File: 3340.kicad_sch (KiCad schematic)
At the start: 176 parts, among them J1 Conn_01x17, J10 FM1, J11 Conn_01x17, J12 V/OCT2, J13 PULSE2, J14 SAW2, J15 TRI2, J16 SINE2, J17 SYNC2, J18 Conn_01x17, J19 PWM2, J2 Conn_01x17, J20 FM2, J3 V/OCT1, J4 PULSE1, J5 SAW1, J6 TRI1, J7 SINE1, J8 SYNC1, J9 PWM1, Q1 2N3904, Q2 2N3906, Q3 2N3904, Q4 2N3906, Q5 2N3904, Q6 2N3904, SW2 DPDT_OOO, U1 TL072, U2 TL074, U3 CEM3340, U4 TL072, U5 CEM3340, U6 TL074

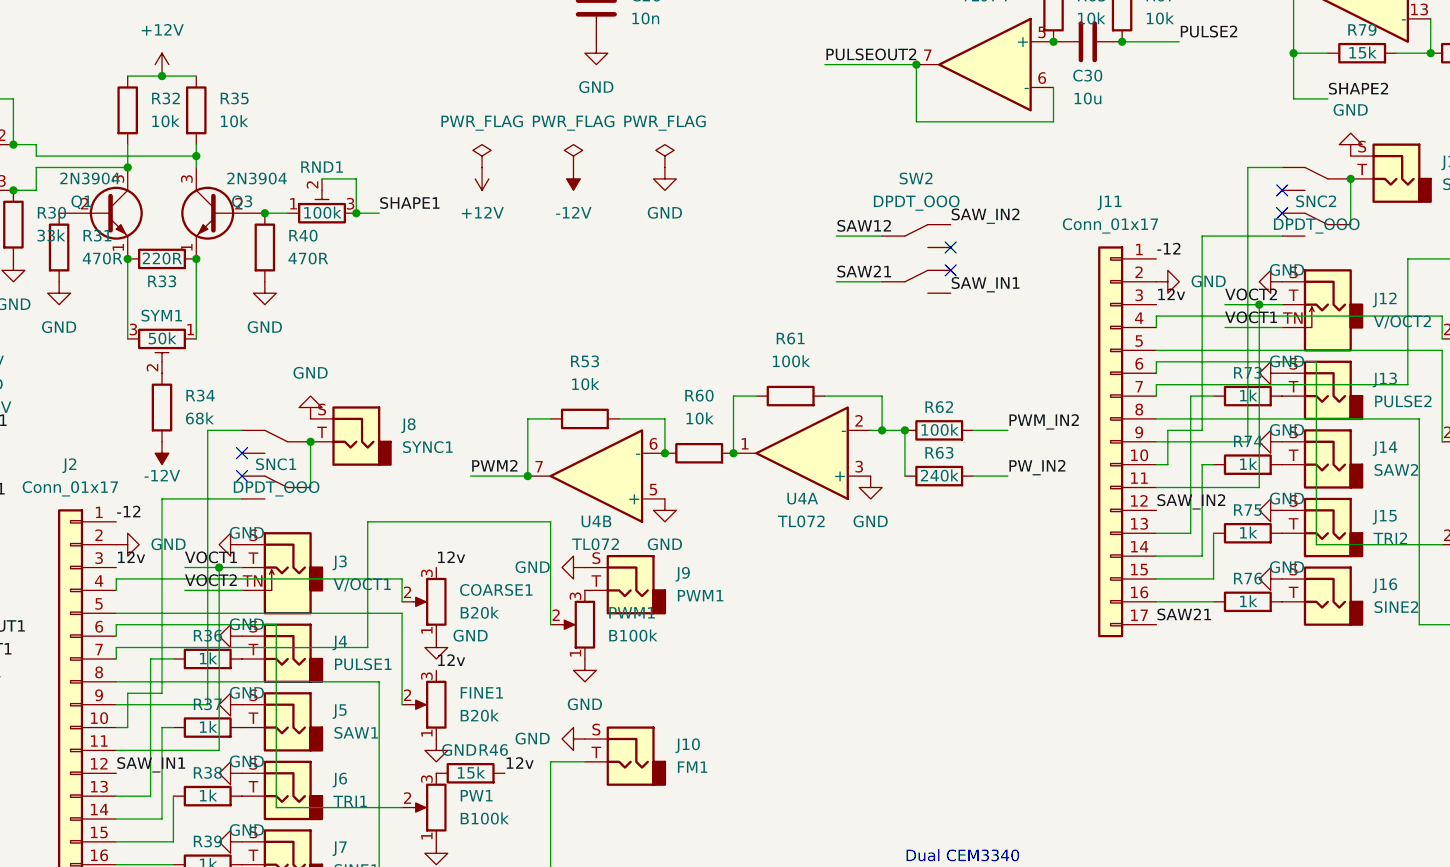
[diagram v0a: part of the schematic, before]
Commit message: Fix synch switches in schematic
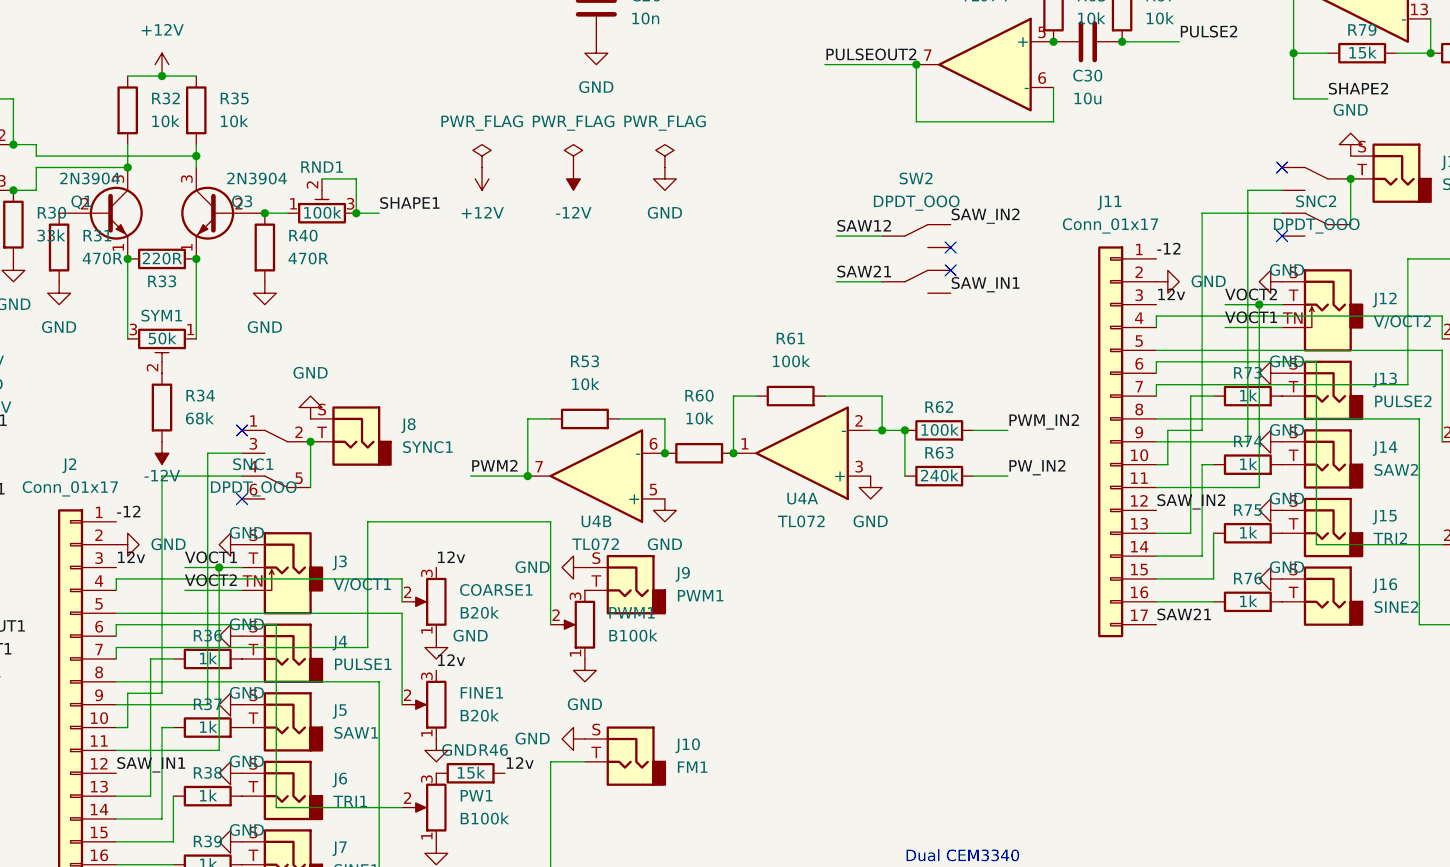
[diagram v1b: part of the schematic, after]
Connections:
- net at SNC2.1: no longer J11.9 (Pin_9)
- net at SNC2.3: now also J11.9 (Pin_9)
- net at SNC2.4: now also J11.10 (Pin_10)
- net at SNC2.6: no longer J11.10 (Pin_10)
- net at J2.10 (Pin_10): now also SNC1.4; no longer SNC1.6
- net at J2.9 (Pin_9): now also SNC1.3; no longer SNC1.1
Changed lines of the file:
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@@
   (junction (at 149.86 83.82) (diameter 0) (color 0 0 0 0)
   )
-  (no_connect (at 113.03 144.78))
-  (no_connect (at 113.03 147.32))
-  (no_connect (at 228.6 115.57))
-  (no_connect (at 228.6 118.11))
+  (no_connect (at 113.03 149.86))
+  (no_connect (at 228.6 113.03))
+  (no_connect (at 113.03 142.24))
+  (no_connect (at 228.6 120.65))
   (no_connect (at 191.77 121.92))
   (no_connect (at 191.77 124.46))
@@
     (stroke (width 0) (type default) (color 0 0 0 0))
   )
+  (wire (pts (xy 224.79 115.57) (xy 228.6 115.57))
+    (stroke (width 0) (type default) (color 0 0 0 0))
+  )
   (wire (pts (xy 15.24 138.43) (xy 24.13 138.43))
     (stroke (width 0) (type default) (color 0 0 0 0))
@@
     (stroke (width 0) (type default) (color 0 0 0 0))
   )
-  (wire (pts (xy 109.22 142.24) (xy 113.03 142.24))
-    (stroke (width 0) (type default) (color 0 0 0 0))
-  )
   (wire (pts (xy 57.15 182.88) (xy 58.42 182.88))
     (stroke (width 0) (type default) (color 0 0 0 0))
@@
     (stroke (width 0) (type default) (color 0 0 0 0))
   )
+  (wire (pts (xy 224.79 143.51) (xy 224.79 115.57))
+    (stroke (width 0) (type default) (color 0 0 0 0))
+  )
   (wire (pts (xy 64.77 81.28) (xy 67.31 81.28))
     (stroke (width 0) (type default) (color 0 0 0 0))
   )
+  (wire (pts (xy 219.71 118.11) (xy 228.6 118.11))
+    (stroke (width 0) (type default) (color 0 0 0 0))
+  )
   (wire (pts (xy 67.31 45.72) (xy 67.31 69.85))
     (stroke (width 0) (type default) (color 0 0 0 0))
@@
     (stroke (width 0) (type default) (color 0 0 0 0))
   )
-  (wire (pts (xy 224.79 113.03) (xy 228.6 113.03))
-    (stroke (width 0) (type default) (color 0 0 0 0))
-  )
   (wire (pts (xy 189.23 50.8) (xy 194.31 50.8))
     (stroke (width 0) (type default) (color 0 0 0 0))
@@
     (stroke (width 0) (type default) (color 0 0 0 0))
   )
-  (wire (pts (xy 219.71 142.24) (xy 219.71 120.65))
+  (wire (pts (xy 219.71 118.11) (xy 219.71 142.24))
     (stroke (width 0) (type default) (color 0 0 0 0))
   )
@@
     (stroke (width 0) (type default) (color 0 0 0 0))
   )
-  (wire (pts (xy 109.22 172.72) (xy 109.22 142.24))
-    (stroke (width 0) (type default) (color 0 0 0 0))
-  )
   (wire (pts (xy 214.63 140.97) (xy 243.84 140.97))
     (stroke (width 0) (type default) (color 0 0 0 0))
   )
-  (wire (pts (xy 219.71 120.65) (xy 228.6 120.65))
-    (stroke (width 0) (type default) (color 0 0 0 0))
-  )
   (wire (pts (xy 60.96 35.56) (xy 63.5 35.56))
     (stroke (width 0) (type default) (color 0 0 0 0))
@@
     (stroke (width 0) (type default) (color 0 0 0 0))
   )
-  (wire (pts (xy 104.14 171.45) (xy 104.14 149.86))
+  (wire (pts (xy 104.14 147.32) (xy 104.14 171.45))
     (stroke (width 0) (type default) (color 0 0 0 0))
   )
@@
     (stroke (width 0) (type default) (color 0 0 0 0))
   )
+  (wire (pts (xy 109.22 144.78) (xy 113.03 144.78))
+    (stroke (width 0) (type default) (color 0 0 0 0))
+  )
+  (wire (pts (xy 104.14 147.32) (xy 113.03 147.32))
+    (stroke (width 0) (type default) (color 0 0 0 0))
+  )
   (wire (pts (xy 64.77 71.12) (xy 64.77 76.2))
     (stroke (width 0) (type default) (color 0 0 0 0))
@@
     (stroke (width 0) (type default) (color 0 0 0 0))
   )
+  (wire (pts (xy 109.22 172.72) (xy 109.22 144.78))
+    (stroke (width 0) (type default) (color 0 0 0 0))
+  )
   (wire (pts (xy 219.71 156.21) (xy 219.71 146.05))
     (stroke (width 0) (type default) (color 0 0 0 0))
@@
     (stroke (width 0) (type default) (color 0 0 0 0))
   )
-  (wire (pts (xy 224.79 143.51) (xy 224.79 113.03))
-    (stroke (width 0) (type default) (color 0 0 0 0))
-  )
   (wire (pts (xy 217.17 99.06) (xy 210.82 99.06))
     (stroke (width 0) (type default) (color 0 0 0 0))
@@
   )
   (wire (pts (xy 44.45 24.13) (xy 52.07 24.13))
-    (stroke (width 0) (type default) (color 0 0 0 0))
-  )
-  (wire (pts (xy 104.14 149.86) (xy 113.03 149.86))
     (stroke (width 0) (type default) (color 0 0 0 0))
   )
@@
     (pin "3")
   )
-  (symbol (lib_id "Switch:SW_DPDT") (at 115.57 146.05 0) (mirror y) (unit 1)
-    (in_bom yes) (on_board yes)
-    (property "Reference" "SNC1" (id 0) (at 116.84 146.05 0))
-    (property "Value" "DPDT_OOO" (id 1) (at 116.84 148.59 0))
-    (property "Footprint" "Button_Switch_THT:SW_DPDT_Toggle_Miniature_Lug" (id 2) (at 116.84 146.05 0)
-      (effects (font (size 1.27 1.27)) hide)
-    )
-    (property "Datasheet" "" (id 3) (at 116.84 146.05 0)
-      (effects (font (size 1.27 1.27)) hide)
-    )
+  (symbol (lib_name "SW_DPDT_1") (lib_id "Switch:SW_DPDT") (at 115.57 146.05 0) (mirror y) (unit 1)
+    (in_bom yes) (on_board yes)
+    (property "Reference" "SNC1" (id 0) (at 114.3 146.05 0))
+    (property "Value" "DPDT_OOO" (id 1) (at 114.3 148.59 0))
+    (property "Footprint" "Button_Switch_THT:SW_DPDT_Toggle_Miniature_Lug" (id 2) (at 114.3 146.05 0)
+      (effects (font (size 1.27 1.27)) hide)
+    )
+    (property "Datasheet" "" (id 3) (at 114.3 146.05 0)
+      (effects (font (size 1.27 1.27)) hide)
+    )
